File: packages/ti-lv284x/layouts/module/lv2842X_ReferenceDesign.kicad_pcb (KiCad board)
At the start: 2 copper layers, 8 parts, among them U3 10µH ±20%

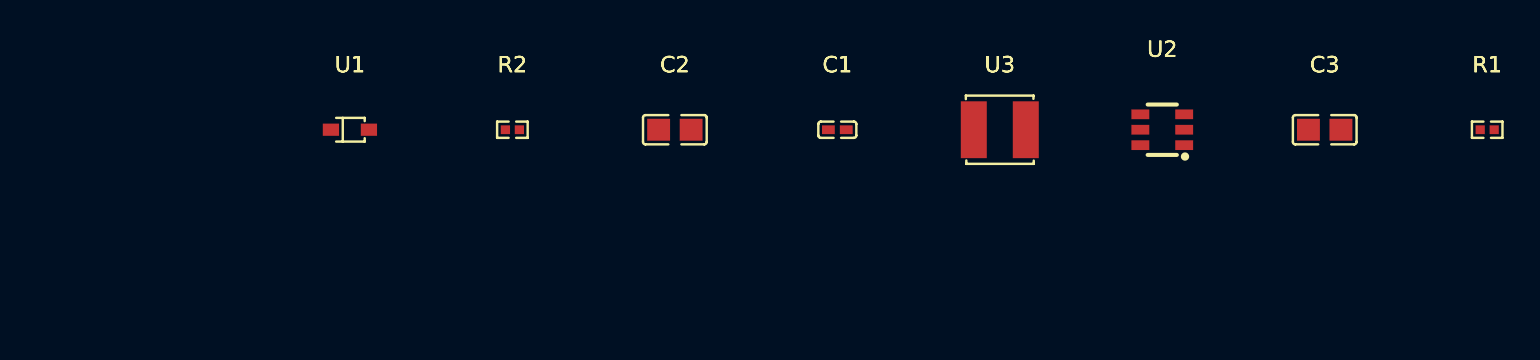
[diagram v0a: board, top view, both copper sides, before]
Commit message: Fix ti-lv284x to build
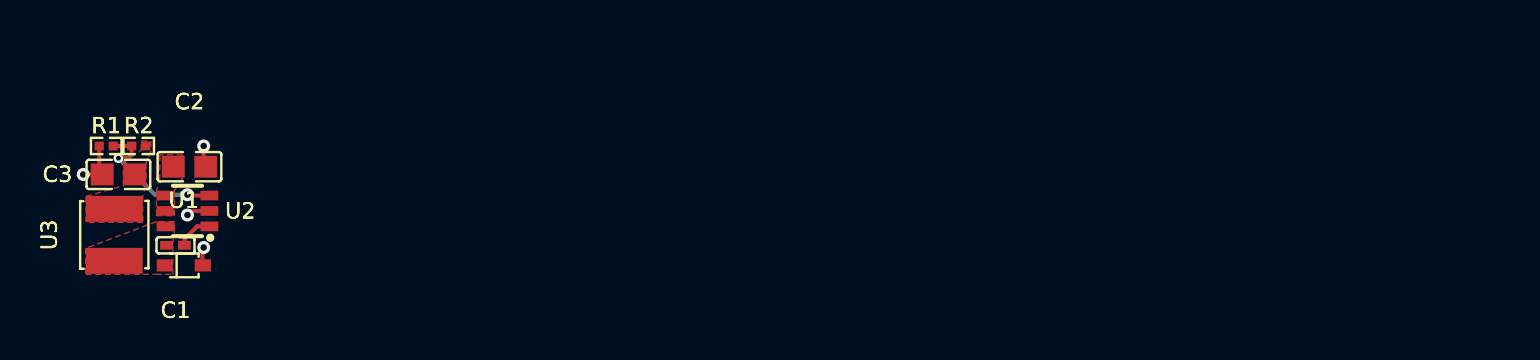
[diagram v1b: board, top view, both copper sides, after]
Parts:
- R2: value 33kΩ ±1% 62.5mW -> 10kΩ ±1% 62.5mW
- moved R1 85.0 mm to (-5.00, -4.00), turned to 180 degrees
- moved C3 74.3 mm to (-4.25, -2.25), turned to 180 degrees
- moved U2 60.2 mm to (0.00, 0.00)
- moved U3 54.9 mm to (-4.50, 1.47), turned to 90 degrees
- moved C1 41.4 mm to (-0.74, 2.11), turned to 180 degrees
- moved C2 30.0 mm to (0.12, -2.73)
- moved R2 23.0 mm to (-3.00, -4.00), turned to 180 degrees
- moved U1 13.2 mm to (-0.23, 3.35)
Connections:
- net hv-1 renamed VIN
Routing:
- net FB: track 0.00 -> 9.13 mm, vias 0 -> 2
- net gnd: track 0.00 -> 4.28 mm, vias 0 -> 2
- net gnd-1: track 0.00 -> 2.70 mm, vias 0 -> 2
- net CB: track 0.00 -> 2.36 mm
- added copper zone on F.Cu, net (none)
